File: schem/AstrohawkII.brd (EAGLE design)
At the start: 64 x 56 mm, 3 parts, among them J1 RASPBERRYPI-40-PIN-GPIO_PTH_N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

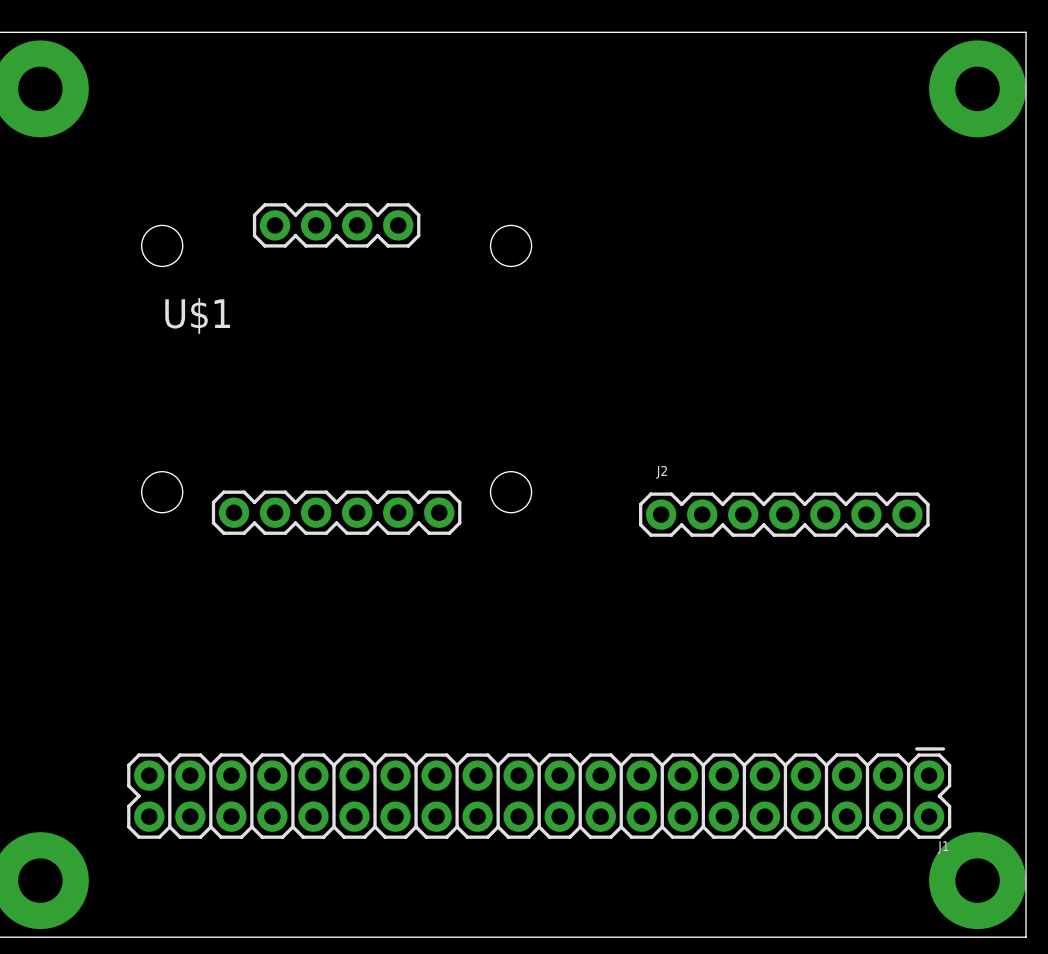
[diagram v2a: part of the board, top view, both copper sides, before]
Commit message: finishes placement and routes wires
This change places the raspberry pi header in the
correct location. It also routes wires to all
relevant locations. For some reason the raspberry
pi header we're using wants to connect all of the
power and ground pins together, but that shouldn't
be necessary, so I've left them unconnected and
they show as air wires.
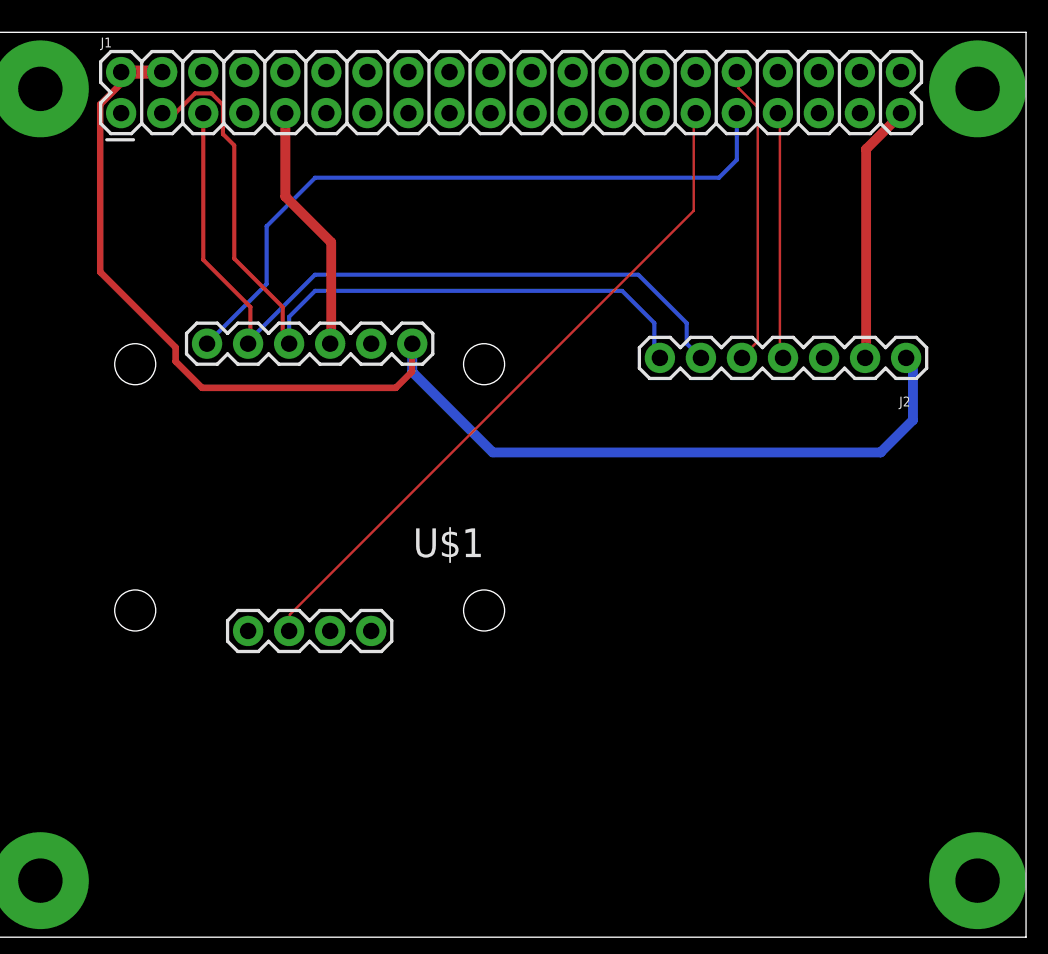
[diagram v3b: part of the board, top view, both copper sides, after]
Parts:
- moved J1 64.7 mm to (8.00, 51.0), turned to 0 degrees
- moved U$1 28.2 mm to (33.0, 38.0), turned to 180 degrees
- moved J2 18.0 mm to (56.6, 35.9), turned to 180 degrees
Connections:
- removed net ADR: U$1.ADR
- removed net PS0: U$1.PS0
- removed net PS1: U$1.PS1
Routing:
- net VIN: track 0.00 -> 80.2 mm
- net SDA: track 0.00 -> 49.3 mm
- net SCL: track 0.00 -> 48.7 mm
- net RST: track 0.00 -> 42.5 mm
- net INT: track 0.00 -> 42.5 mm
- net GND: track 0.00 -> 31.8 mm
- net INT1: track 0.00 -> 18.6 mm
- net INT2: track 0.00 -> 15.3 mm
- net 3.3V: track 0.00 -> 0.99 mm

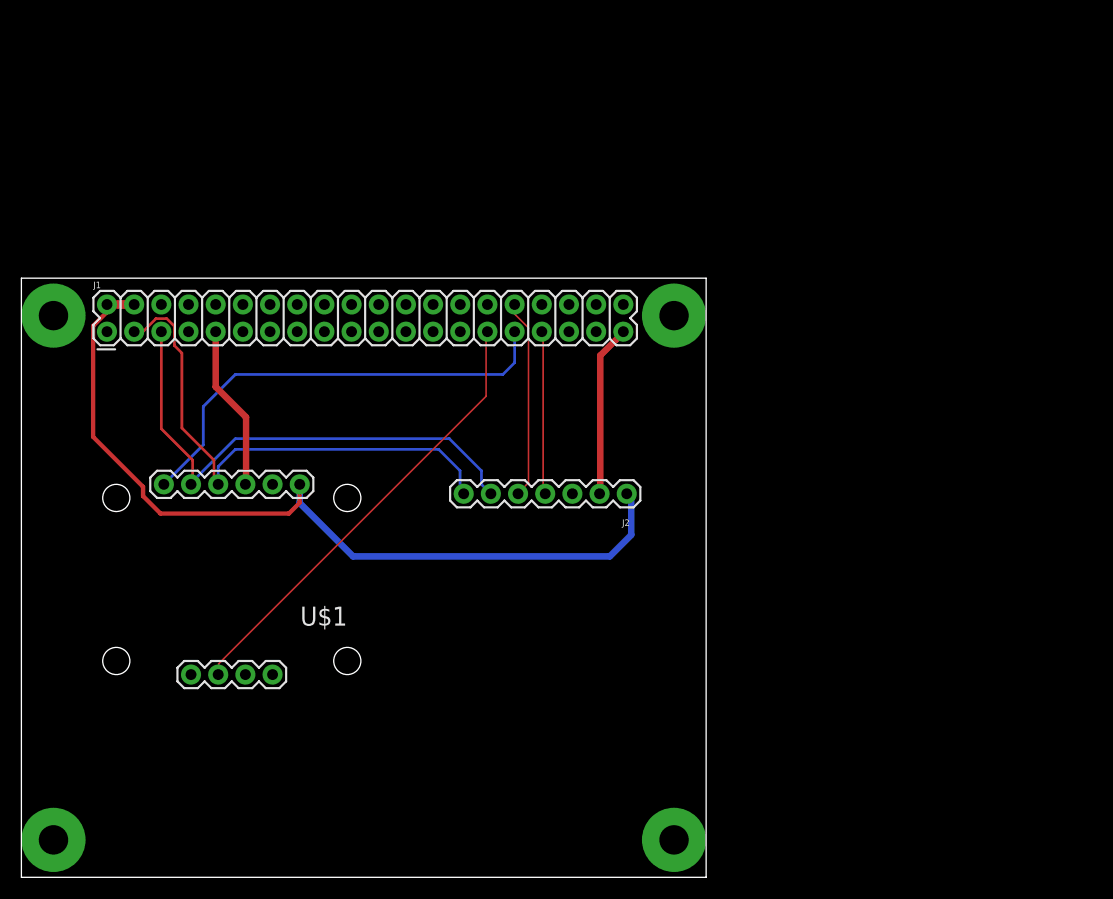
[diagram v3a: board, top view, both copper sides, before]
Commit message: adds finishing touches to pcb design
1. Altimeter device (package/symbol) added with drill holes for screws
2. Drill holes and silk screen updated for IMU device
3. Hole cutout added to account for the camera cable
4. Copper re-routed for Altimeter
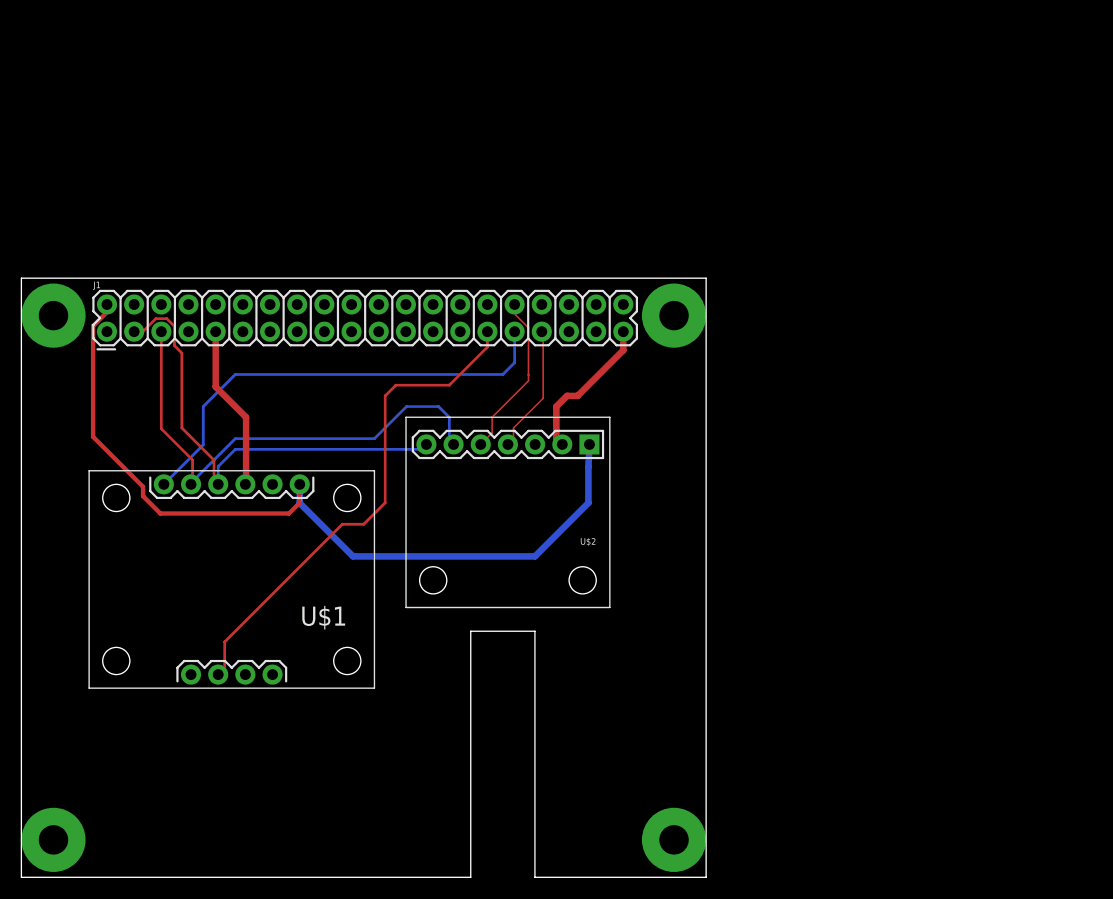
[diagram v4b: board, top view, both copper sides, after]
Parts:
- removed J2: (no value), SparkFun-Connectors:1X07
- added U$2: MPL3115A2, rocketry:MPL3115A2
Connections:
- net GND: now also U$2.GND; no longer J2.2
- net INT1: now also U$2.INT1; no longer J2.5
- net INT2: now also U$2.INT2; no longer J2.4
- net SCL: now also U$2.SCL; no longer J2.6
- net SDA: now also U$2.SDA; no longer J2.7
- net VIN: now also U$2.VIN; no longer J2.1
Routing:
- net SDA: track 49.3 -> 43.1 mm
- net INT: track 42.5 -> 46.6 mm
- net VIN: track 80.2 -> 76.3 mm
- net INT2: track 15.3 -> 12.0 mm
- net INT1: track 18.6 -> 15.6 mm
- net SCL: track 48.7 -> 46.2 mm
- net GND: track 31.8 -> 29.4 mm
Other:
- outline, holes or cut-outs redrawn
